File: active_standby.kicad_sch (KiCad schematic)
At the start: 24 parts, among them Q10 BSS138, Q11 BSS138, Q2 BSS138, Q8 BSS138, Q9 BSS138, U24 SN3257QDYYRQ1, U30 SN3257QDYYRQ1

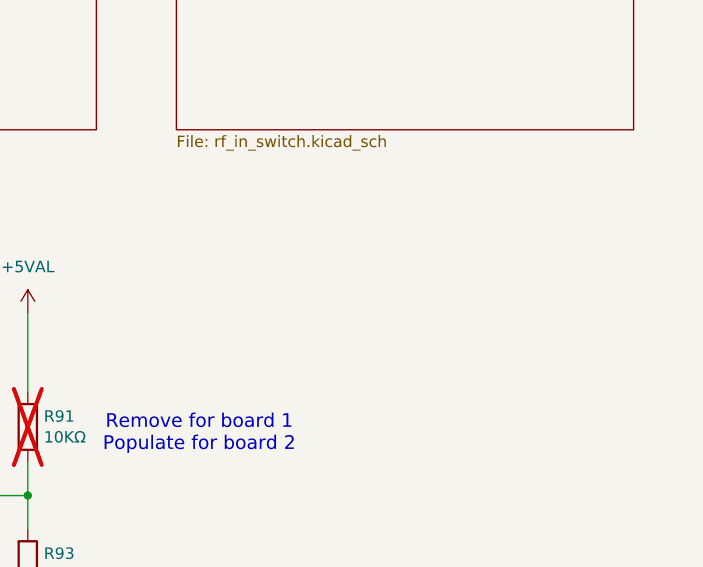
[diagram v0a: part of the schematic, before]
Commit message: Add an optional diplexed antenna input
Signed-off-by: Corey Minyard <corey@minyard.net>
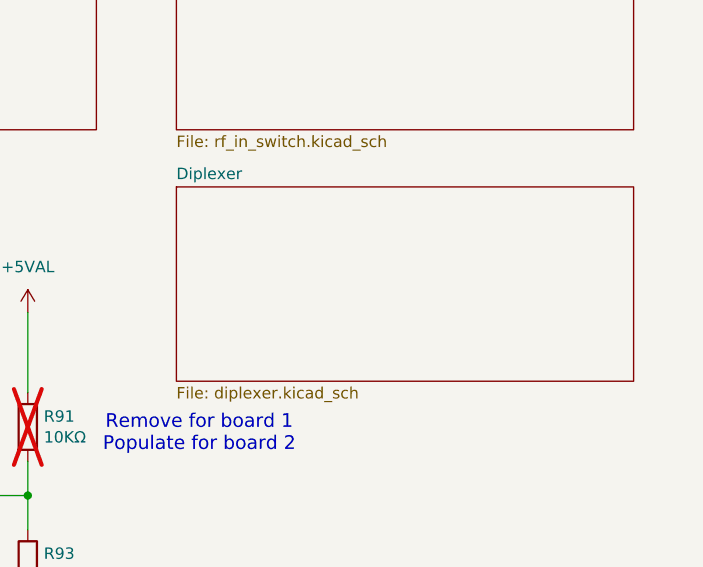
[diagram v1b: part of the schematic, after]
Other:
- added sheet Diplexer (diplexer.kicad_sch)
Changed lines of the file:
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@@
+	)
+	(sheet
+		(at 227.33 46.99)
+		(size 50.8 21.59)
+		(exclude_from_sim no)
+		(in_bom yes)
+		(on_board yes)
+		(dnp no)
+		(fields_autoplaced yes)
+		(stroke
+			(width 0.1524)
+			(type solid)
+		)
+		(fill
+			(color 0 0 0 0.0000)
+		)
+		(property "Sheetname" "Diplexer"
+			(at 227.33 46.2784 0)
+			(effects
+				(font
+					(size 1.27 1.27)
+				)
+				(justify left bottom)
+			)
+		)
+		(property "Sheetfile" "diplexer.kicad_sch"
+			(at 227.33 69.1646 0)
+			(effects
+				(font
+					(size 1.27 1.27)
+				)
+				(justify left top)
+			)
+		)
+		(instances
+			(project "PacSat_AFSK"
+				(path "/cc9f42d2-6985-41ac-acab-5ab7b01c5b38/4fa888af-703c-49ed-93bb-d56d2f02c470"
+					(page "19")
+				)
+			)
+		)
 	)
 	(sheet

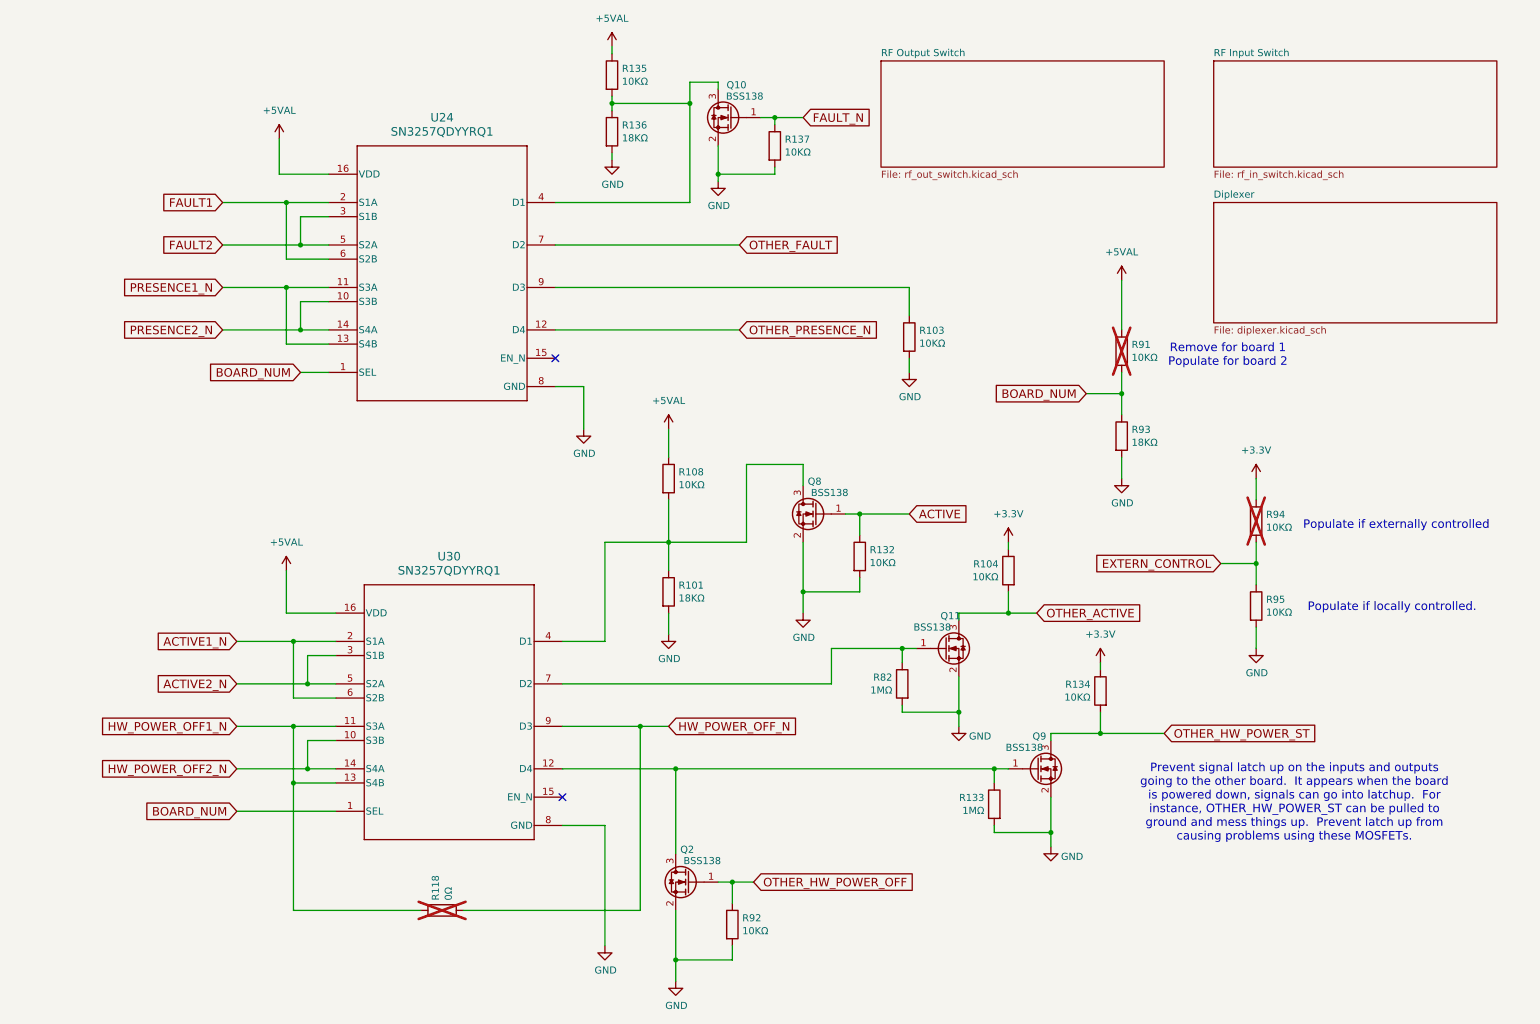
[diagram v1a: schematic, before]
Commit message: Fix issues with some active/standby pins
There were some wrong pullups and pulldowns.

Remove some unnecessary pullups and pulldowns and use the ones
in the CPU instead.

Signed-off-by: Corey Minyard <corey@minyard.net>
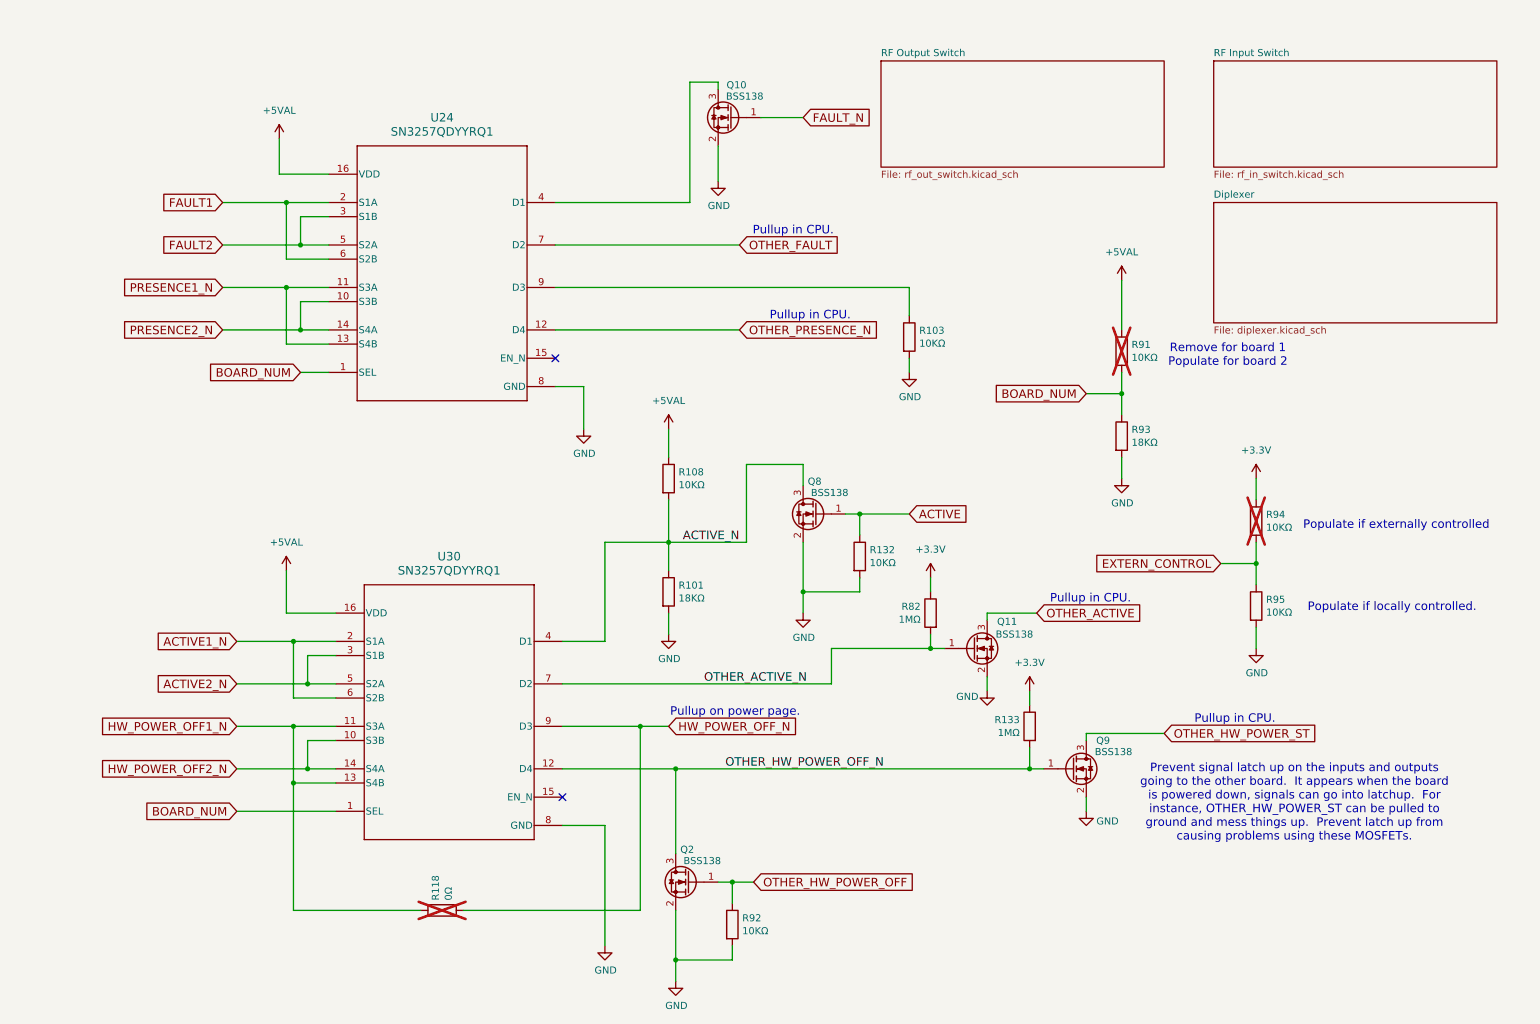
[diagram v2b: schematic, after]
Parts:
- removed R104, R134, R135, R137: 10KΩ, Resistor_SMD:R_0402_1005Metric_Pad0.72x0.64mm_HandSolder, symbol Device:R
- removed R136: 18KΩ, Resistor_SMD:R_0402_1005Metric_Pad0.72x0.64mm_HandSolder, symbol Device:R
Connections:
- net +3.3V: now also R133.1, R82.1
- net GND: no longer R133.2, R82.2
- net OTHER_HW_POWER_OFF_N: now reaches Q2.3 (D), Q9.1 (G), U30.12 (D4)
- net OTHER_HW_POWER_OFF_N: now also R133.2; no longer R133.1
- net ACTIVE_N: now reaches Q8.3 (D), R101.1, R108.2, U30.4 (D1)
- net OTHER_ACTIVE_N: now reaches Q11.1 (G), U30.7 (D2)
- net OTHER_ACTIVE_N: now also R82.2; no longer R82.1
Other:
- note added: "Pullup in CPU."
- note added: "Pullup on power page."
- moved on the sheet: Q11, Q9, R133, R82

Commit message: Add a weak pullup to OTHER_PRESENCE_N
Don't use the processor pullup, their values are not documented and
experience shows they can vary a lot.  We want the other presense
to win if it's there.

Signed-off-by: Corey Minyard <corey@minyard.net>
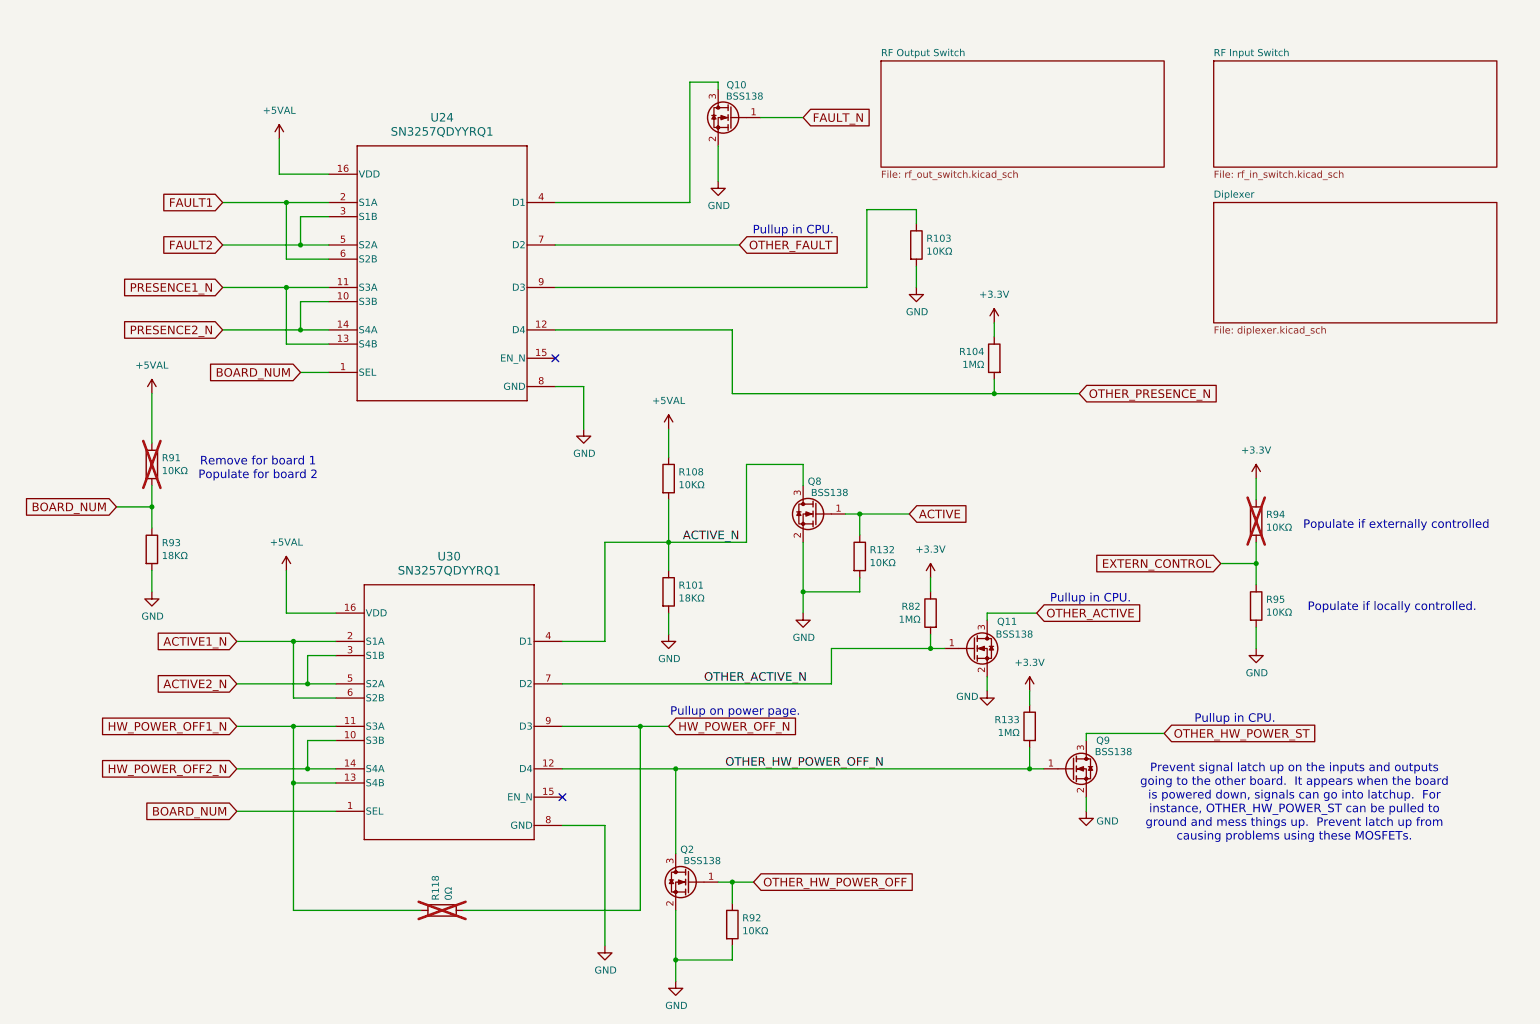
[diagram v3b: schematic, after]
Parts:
- added R104: 1MΩ, Resistor_SMD:R_0402_1005Metric_Pad0.72x0.64mm_HandSolder, symbol Device:R
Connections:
- net +3.3V: now also R104.1
- net OTHER_PRESENCE_N: now also R104.2
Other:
- moved on the sheet: R103, R91, R93
